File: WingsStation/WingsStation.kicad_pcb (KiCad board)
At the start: 2 copper layers, 90.1 x 71.4 mm, 57 parts, among them J1 String1, J10 SWD, J11 SD Card, J2 String2, J3 String3, J4 String4, J5 OLED, J6 VIN_Voltage, J7 RJ45, J8 Buttons, J9 Debug, SW4 RUN, U1 Pico, U2 AMS1117-5.0, U4 74AHCT1G125, U5 74AHCT1G125, U6 74AHCT1G125, U7 74AHCT1G125

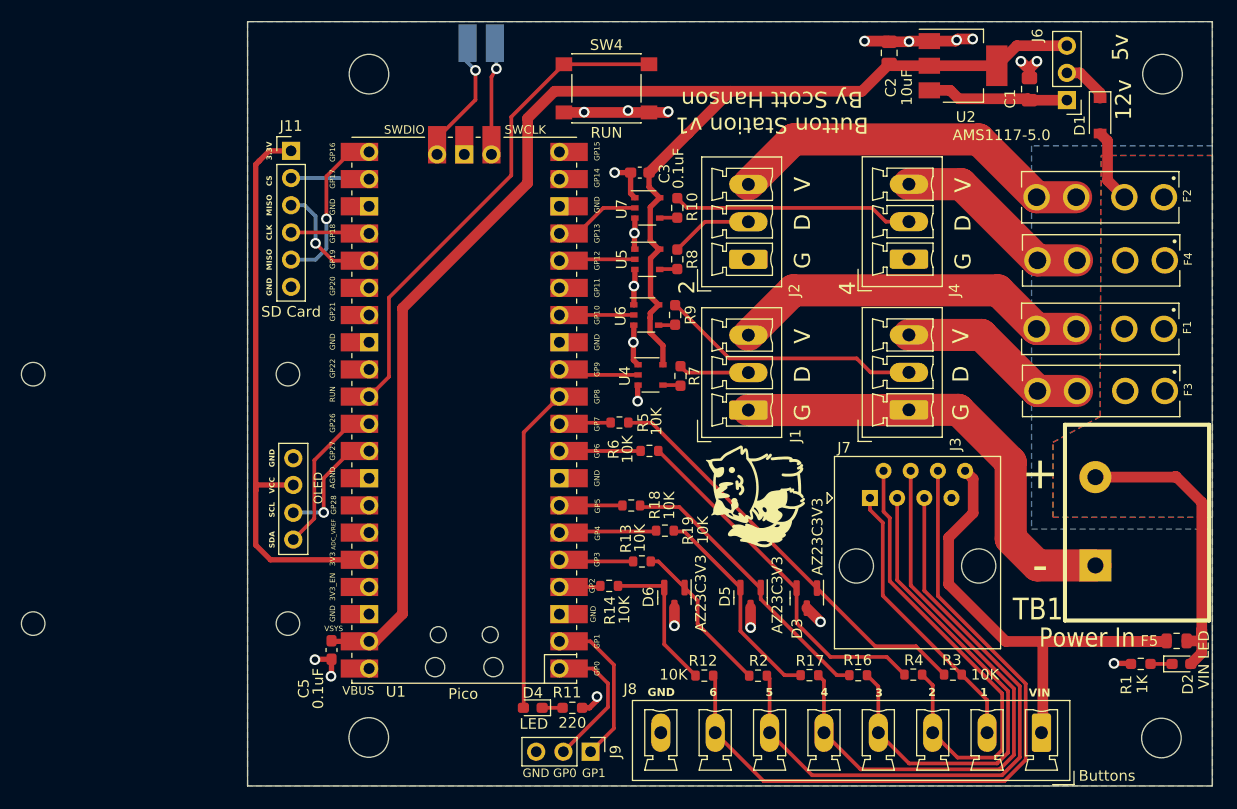
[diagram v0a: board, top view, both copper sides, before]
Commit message: fix pinout
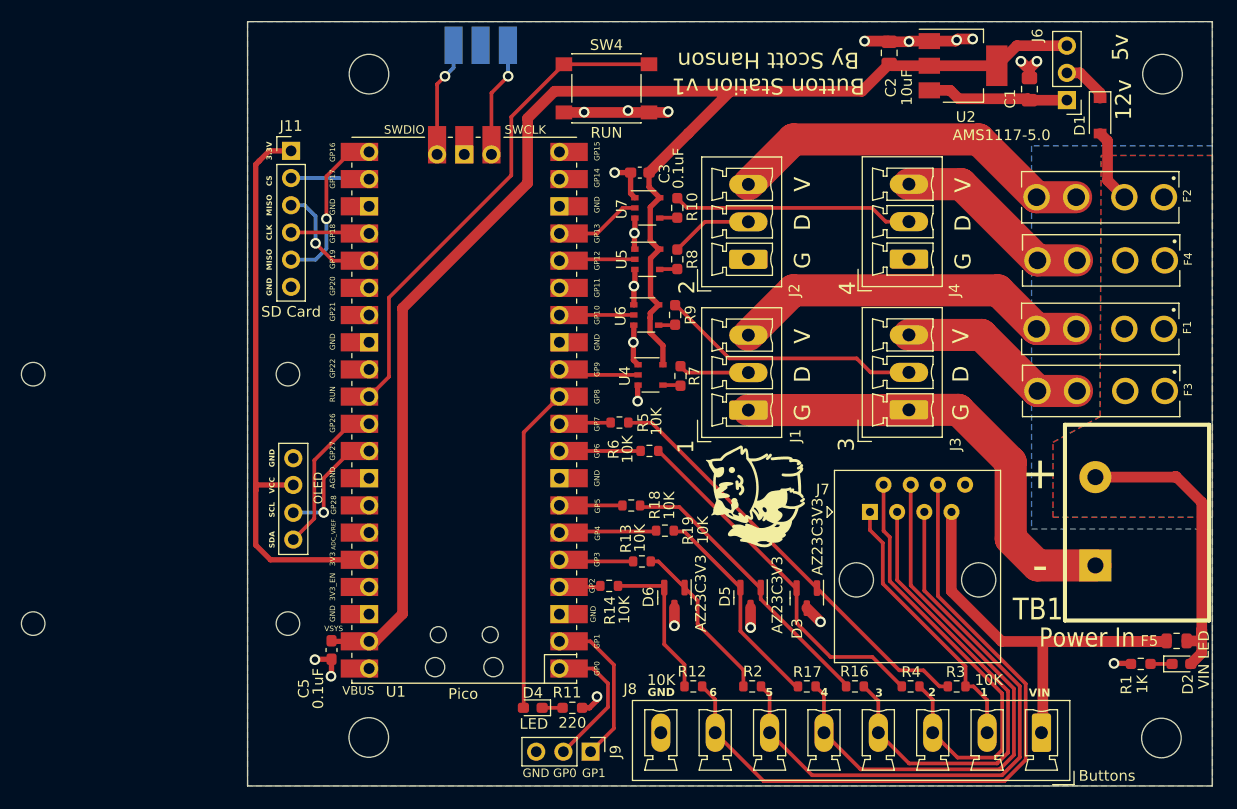
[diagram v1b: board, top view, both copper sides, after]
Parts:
- F5: value Fuse_Small -> Button_Fuse
- J10: footprint Scotts:1x02_Horizontal_SMD -> Scotts:1x03_Horizontal_SMD
- moved R12 1.44 mm to (79.6, 143.9)
- moved J7 1.30 mm to (96.1, 127.6)
- moved J10 1.24 mm to (64.8, 83.1)
- moved R3 1.15 mm to (104.2, 143.9)
- moved R2 1.14 mm to (85.1, 143.9)
- moved R4 1.13 mm to (99.9, 143.9)
- moved R16 1.09 mm to (94.7, 143.9)
- moved R17 1.08 mm to (90.2, 143.9)
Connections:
- J10 pad 2: /Micro/SWDIO -> GND
- J7 pad 7: GND -> B_PWR
- J7 pad 8: B_PWR -> GND
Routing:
- net B_PWR: track 54.5 -> 49.6 mm
- net IN1: track 44.3 -> 42.0 mm
- net IN3: track 55.9 -> 53.6 mm
- net IN2: track 47.6 -> 45.4 mm
- net IN4: track 59.1 -> 57.0 mm
- net IN5: track 67.5 -> 65.6 mm
- net /Micro/SWDIO: track 13.2 -> 11.7 mm
- net IN0: track 26.5 -> 25.6 mm
- net Net-(D3-K-Pad1): track 39.3 -> 40.1 mm
- net Net-(D6-K-Pad1): track 14.9 -> 15.7 mm
- net Net-(D6-K-Pad2): track 13.8 -> 14.4 mm

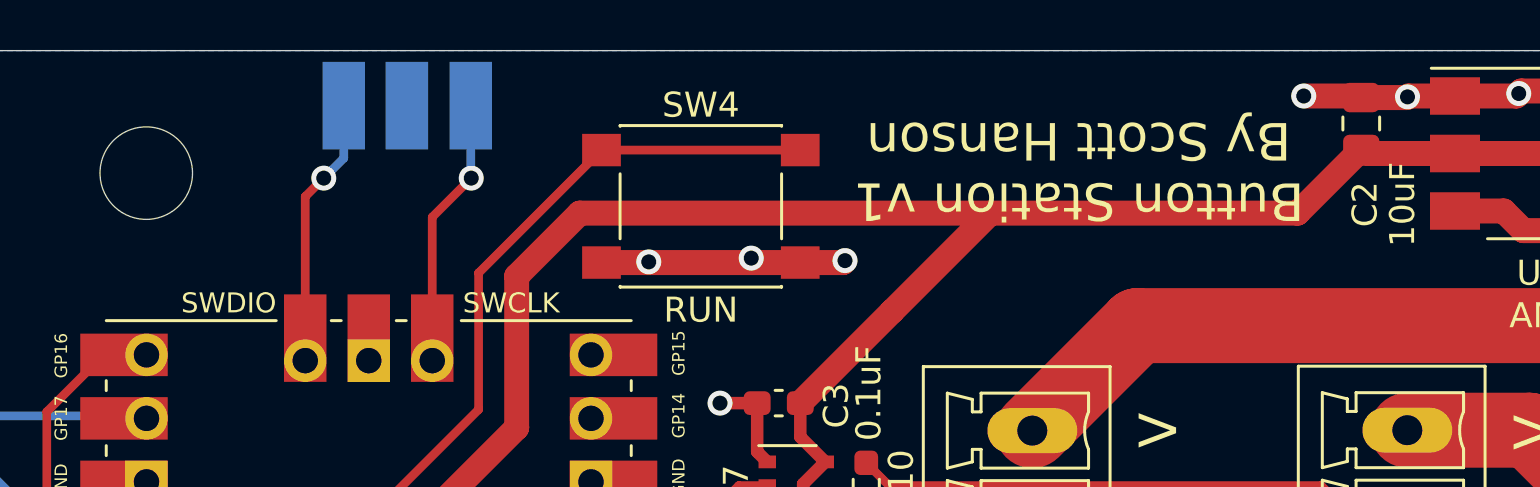
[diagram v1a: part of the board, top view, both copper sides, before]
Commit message: update to expansions, add pico button board
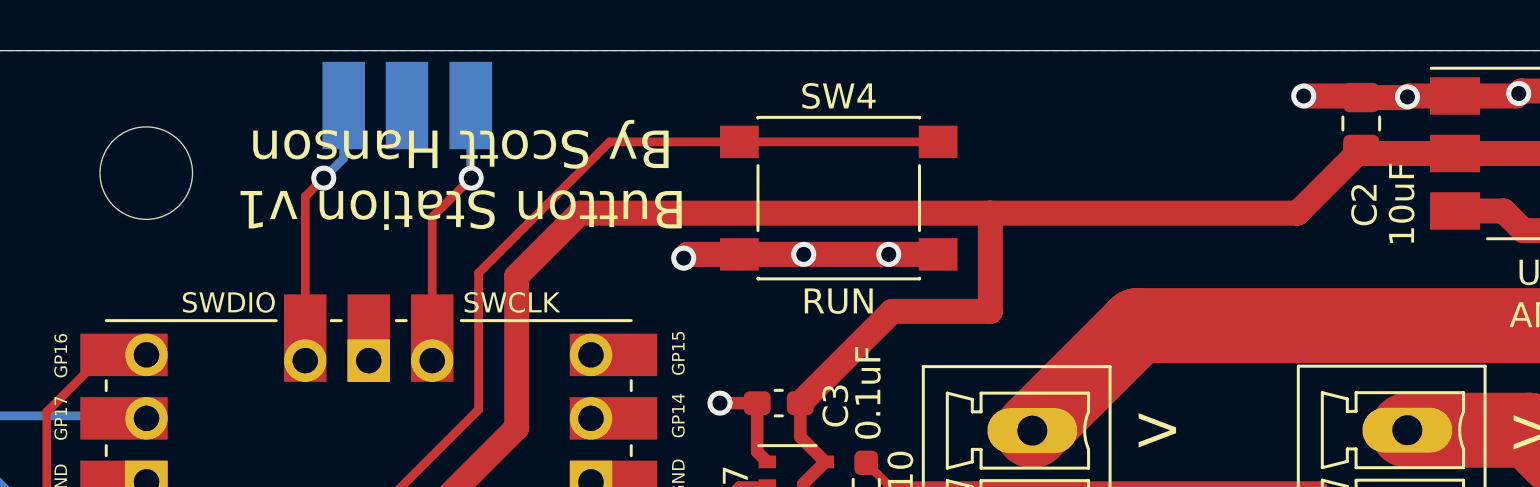
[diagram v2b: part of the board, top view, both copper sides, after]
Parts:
- moved SW4 5.53 mm to (77.0, 87.7)
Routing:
- net Net-(U1-RUN): track 46.5 -> 52.2 mm
- net +5V: track 143.4 -> 145.7 mm
